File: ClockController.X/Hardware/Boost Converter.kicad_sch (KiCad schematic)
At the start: 9 parts, among them J2 HDR-1X2H, Q2 FDD7N25LZTM, Q3 MMBT2222A-TP, Q4 MMBT2907ALT1G

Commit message: Updated most footprints
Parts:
- C3: footprint Clock Controller:CAP_1206 -> Capacitor_SMD:C_1206_3216Metric
- D1: value DSS120U -> SMD220PL; footprint Clock Controller:SODFL390X160X160L90X160N -> Diode_SMD:D_SOD-123F
- J2: footprint Clock Controller:HDR-1X2H -> Connector_PinHeader_2.54mm:PinHeader_1x02_P2.54mm_Horizontal
- Q2: footprint Clock Controller:DPAK3P457_990X250L129X75T444X550N -> Package_TO_SOT_SMD:TO-252-2; symbol Clock Controller-eagle-import:FDD7N25LZTM -> Transistor_FET_:FDD7N25LZTM
- Q3, Q4: footprint Clock Controller:SOT23-3P95_240X110L43X44N -> Package_TO_SOT_SMD:SOT-23
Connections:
- net GND_DIGITAL: now also Q2.3 (S); no longer Q2.2 (S)
- net at D1.2 (A), L1.2: now also Q2.2 (D); no longer Q2.3 (D)
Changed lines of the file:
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@@
 			)
 		)
-		(property "Footprint" "Clock Controller:HDR-1X2H"
+		(property "Footprint" "Connector_PinHeader_2.54mm:PinHeader_1x02_P2.54mm_Horizontal"
 			(at 118.11 60.96 0)
 			(effects
@@
 			)
 		)
-		(property "Value" "DSS120U"
+		(property "Value" "SMD220PL"
 			(at 160.02 77.47 0)
 			(effects
@@
 			)
 		)
-		(property "Footprint" "Clock Controller:SODFL390X160X160L90X160N"
+		(property "Footprint" "Diode_SMD:D_SOD-123F"
 			(at 160.02 77.47 0)
 			(effects
@@
 	)
 	(symbol
-		(lib_id "Clock Controller-eagle-import:FDD7N25LZTM")
+		(lib_id "Transistor_FET_:FDD7N25LZTM")
 		(at 138.43 118.11 0)
 		(unit 1)
@@
 			)
 		)
-		(property "Footprint" "Clock Controller:DPAK3P457_990X250L129X75T444X550N"
+		(property "Footprint" "Package_TO_SOT_SMD:TO-252-2"
 			(at 138.43 118.11 0)
 			(effects
 				(font
 					(size 1.27 1.27)
-				)
-				(hide yes)
-			)
-		)
-		(property "Datasheet" ""
+					(italic yes)
+				)
+				(hide yes)
+			)
+		)
+		(property "Datasheet" "FDD7N25LZTM"
 			(at 138.43 118.11 0)
 			(effects
 				(font
 					(size 1.27 1.27)
+					(italic yes)
 				)
 				(hide yes)
@@
 			)
 		)
-		(property "Footprint" "Clock Controller:SOT23-3P95_240X110L43X44N"
+		(property "Footprint" "Package_TO_SOT_SMD:SOT-23"
 			(at 113.335 132.652 0)
 			(effects
@@
 			)
 		)
-		(property "Footprint" "Clock Controller:CAP_1206"
+		(property "Footprint" "Capacitor_SMD:C_1206_3216Metric"
 			(at 172.72 100.33 0)
 			(effects
@@
 			)
 		)
-		(property "Footprint" "Clock Controller:SOT23-3P95_240X110L43X44N"
+		(property "Footprint" "Package_TO_SOT_SMD:SOT-23"
 			(at 106.985 104.14 0)
 			(effects

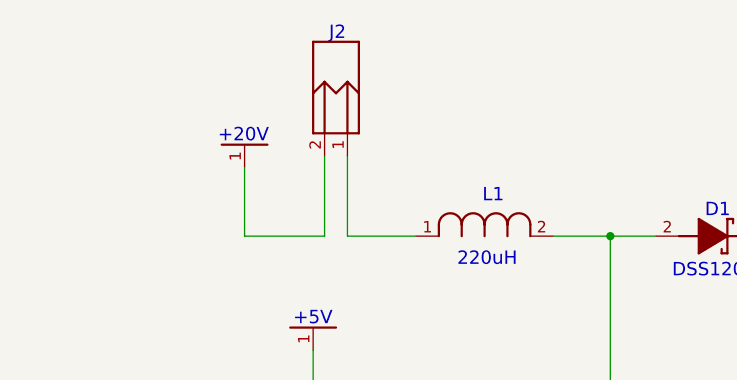
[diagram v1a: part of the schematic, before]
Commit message: Fixing design rule violations
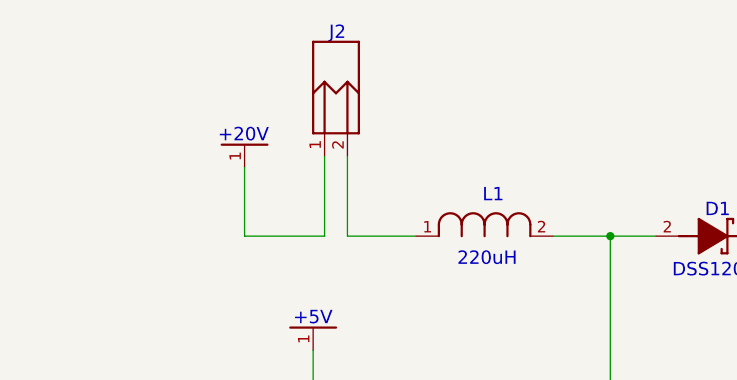
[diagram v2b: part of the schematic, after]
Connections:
- net +20V: now also J2.1 (P1); no longer J2.2 (P2)
- net at L1.1: now also J2.2 (P2); no longer J2.1 (P1)
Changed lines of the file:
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@@
 	(symbol
 		(lib_id "Clock Controller-eagle-import:HDR-1X2H")
-		(at 118.11 60.96 270)
+		(at 118.11 60.96 90)
+		(mirror x)
 		(unit 1)
 		(exclude_from_sim no)

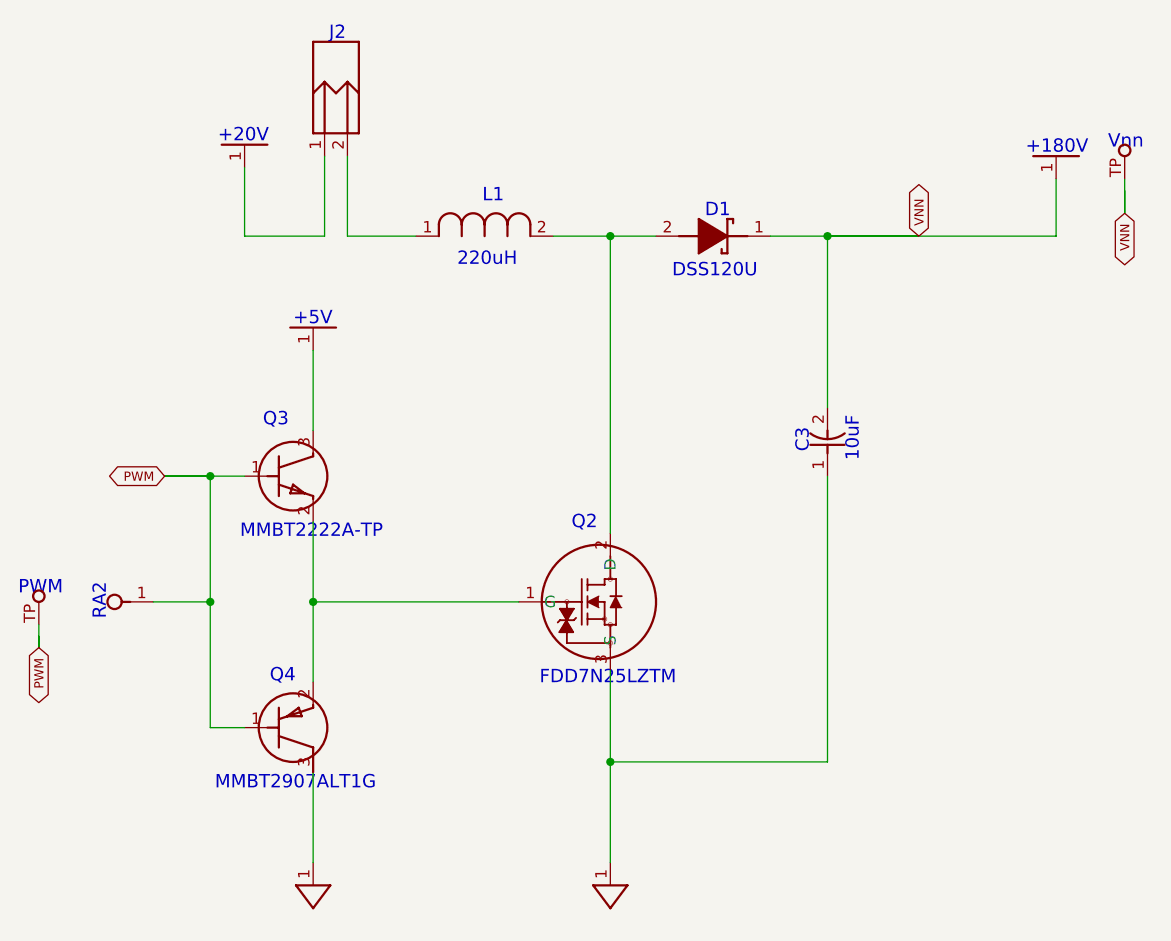
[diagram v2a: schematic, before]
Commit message: Replacing many thin traces with poured zones.
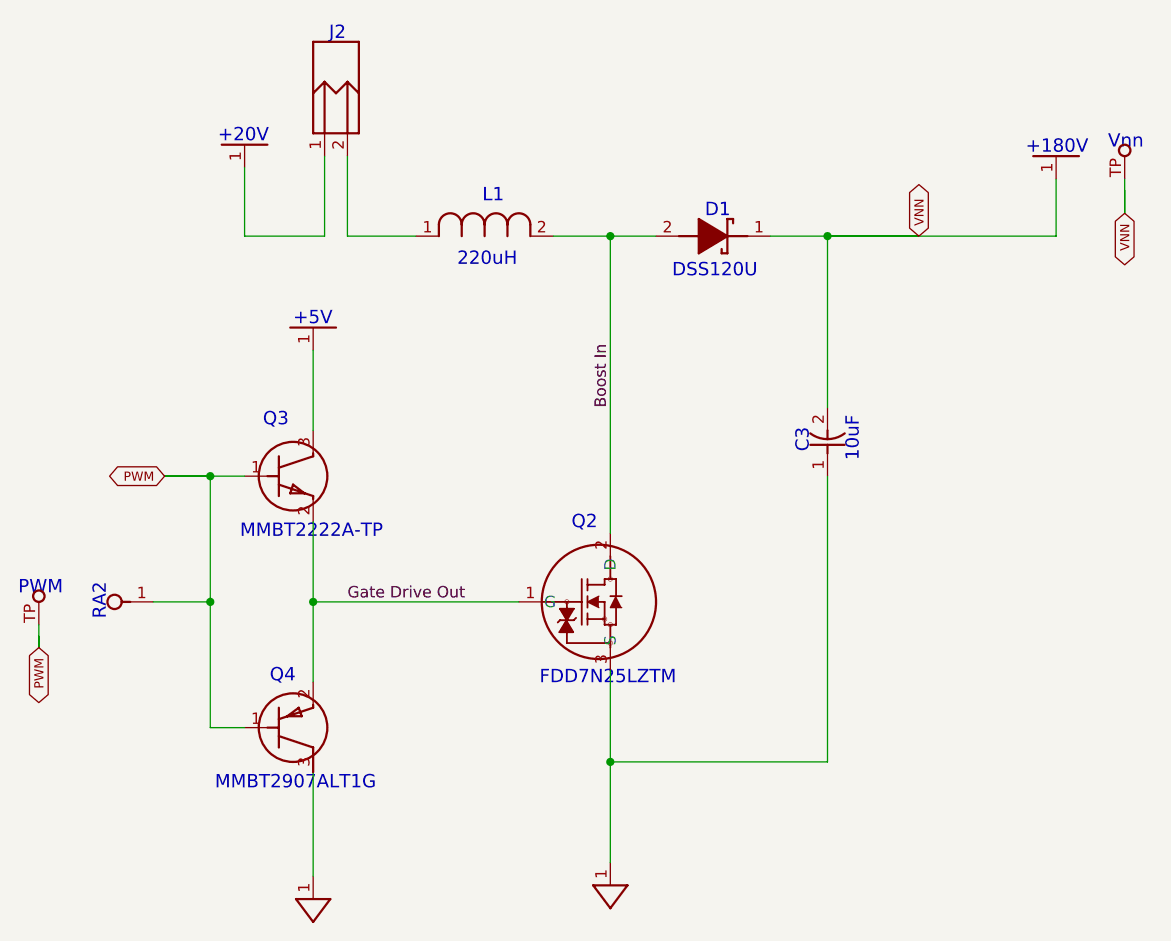
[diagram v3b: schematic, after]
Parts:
- C3: footprint Capacitor_SMD:C_1206_3216Metric -> Capacitor_SMD:C_1812_4532Metric
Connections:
- net GND_DIGITAL: now also Q4.3 (C)
- net Boost In: now reaches D1.2 (A), L1.2, Q2.2 (D)
- net Gate Drive Out: now reaches Q2.1 (G), Q3.2 (E), Q4.2 (E)
